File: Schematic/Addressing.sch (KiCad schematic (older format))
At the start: 6 parts, among them IC10 74LS593, IC11 74LS153, IC7 74LS574, IC8 74LS574, IC9 74LS593, U1 QX14T50B1.843200B50TT

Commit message: Fixed up some schematic DCN mistakes and also a few minor typos and diagram issues.
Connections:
- net labels added: adr[0..15], d[0..7]
- net labels removed: AddressBus, DataBus
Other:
- note added: "AddressBus"
- note added: "DataBus"
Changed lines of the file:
@@
 	5600 5100 5550 5100
 $Comp
-L GNDREF #PWR025
+L GNDREF #PWR020
 U 1 1 5C911F8E
 P 7000 6150
-F 0 "#PWR025" H 7000 5900 50  0001 C CNN
+F 0 "#PWR020" H 7000 5900 50  0001 C CNN
 F 1 "GNDREF" H 7000 6000 50  0000 C CNN
 F 2 "" H 7000 6150 50  0001 C CNN
@@
 $EndComp
 $Comp
-L VCC #PWR026
+L VCC #PWR021
 U 1 1 5C911FB4
 P 7000 6000
-F 0 "#PWR026" H 7000 5850 50  0001 C CNN
+F 0 "#PWR021" H 7000 5850 50  0001 C CNN
 F 1 "VCC" H 7000 6150 50  0000 C CNN
 F 2 "" H 7000 6000 50  0001 C CNN
@@
 $EndComp
 $Comp
-L VCC #PWR027
+L VCC #PWR022
 U 1 1 5C913009
 P 5550 4600
-F 0 "#PWR027" H 5550 4450 50  0001 C CNN
+F 0 "#PWR022" H 5550 4450 50  0001 C CNN
 F 1 "VCC" H 5550 4750 50  0000 C CNN
 F 2 "" H 5550 4600 50  0001 C CNN
@@
 	3000 6150 4450 6150
 $Comp
-L GNDREF #PWR028
+L GNDREF #PWR023
 U 1 1 5C90C705
 P 1800 6250
-F 0 "#PWR028" H 1800 6000 50  0001 C CNN
+F 0 "#PWR023" H 1800 6000 50  0001 C CNN
 F 1 "GNDREF" H 1800 6100 50  0000 C CNN
 F 2 "" H 1800 6250 50  0001 C CNN
@@
 	3000 6450 3200 6450
 $Comp
-L VCC #PWR029
+L VCC #PWR024
 U 1 1 5C90C821
 P 3200 6450
-F 0 "#PWR029" H 3200 6300 50  0001 C CNN
+F 0 "#PWR024" H 3200 6300 50  0001 C CNN
 F 1 "VCC" H 3200 6600 50  0000 C CNN
 F 2 "" H 3200 6450 50  0001 C CNN
@@
 	1    0    0    -1
 $EndComp
-Text GLabel 1250 650  0    60   Input ~ 0
-AddressBus
 $Comp
 L 74LS574-RESCUE-Schematic IC7
@@
 Wire Bus Line
 	1950 4900 1200 4900
-Text GLabel 1200 4900 0    60   Input ~ 0
-DataBus
 Entry Wire Line
 	1950 3300 2050 3200
@@
 d7
 $Comp
-L VCC #PWR035
+L VCC #PWR025
 U 1 1 5C99A807
 P 3850 2150
-F 0 "#PWR035" H 3850 2000 50  0001 C CNN
+F 0 "#PWR025" H 3850 2000 50  0001 C CNN
 F 1 "VCC" H 3850 2300 50  0000 C CNN
 F 2 "" H 3850 2150 50  0001 C CNN
@@
 $EndComp
 $Comp
-L VCC #PWR036
+L VCC #PWR026
 U 1 1 5C99A830
 P 3850 4100
-F 0 "#PWR036" H 3850 3950 50  0001 C CNN
+F 0 "#PWR026" H 3850 3950 50  0001 C CNN
 F 1 "VCC" H 3850 4250 50  0000 C CNN
 F 2 "" H 3850 4100 50  0001 C CNN
@@
 $EndComp
 $Comp
-L GNDREF #PWR038
+L GNDREF #PWR027
 U 1 1 5C99A88B
 P 3850 2250
-F 0 "#PWR038" H 3850 2000 50  0001 C CNN
+F 0 "#PWR027" H 3850 2000 50  0001 C CNN
 F 1 "GNDREF" H 3850 2100 50  0000 C CNN
 F 2 "" H 3850 2250 50  0001 C CNN
@@
 $EndComp
 $Comp
-L GNDREF #PWR039
+L GNDREF #PWR028
 U 1 1 5C99AB18
 P 3850 4200
-F 0 "#PWR039" H 3850 3950 50  0001 C CNN
+F 0 "#PWR028" H 3850 3950 50  0001 C CNN
 F 1 "GNDREF" H 3850 4050 50  0000 C CNN
 F 2 "" H 3850 4200 50  0001 C CNN
@@
 	4100 3800 5650 3800
 Wire Bus Line
-	4000 650  1250 650
+	4000 650  3350 650
 Wire Wire Line
 	4100 1250 5650 1250
@@
 Connection ~ 4400 2150
 $Comp
-L VCC #PWR?
+L VCC #PWR029
 U 1 1 5C9A1A2E
 P 7300 1250
-F 0 "#PWR?" H 7300 1100 50  0001 C CNN
+F 0 "#PWR029" H 7300 1100 50  0001 C CNN
 F 1 "VCC" H 7300 1400 50  0000 C CNN
 F 2 "" H 7300 1250 50  0001 C CNN
@@
 NoConn ~ 7000 1250
 $Comp
-L GNDREF #PWR?
+L GNDREF #PWR030
 U 1 1 5C9A1C76
 P 7300 4200
-F 0 "#PWR?" H 7300 3950 50  0001 C CNN
+F 0 "#PWR030" H 7300 3950 50  0001 C CNN
 F 1 "GNDREF" H 7300 4050 50  0000 C CNN
 F 2 "" H 7300 4200 50  0001 C CNN
@@
 Connection ~ 7300 3600
 $Comp
-L GNDREF #PWR?
+L GNDREF #PWR031
 U 1 1 5C9A1E6F
 P 7300 2050
-F 0 "#PWR?" H 7300 1800 50  0001 C CNN
+F 0 "#PWR031" H 7300 1800 50  0001 C CNN
 F 1 "GNDREF" H 7300 1900 50  0000 C CNN
 F 2 "" H 7300 2050 50  0001 C CNN
@@
 	7450 1950 7450 3900
 $Comp
-L VCC #PWR?
+L VCC #PWR032
 U 1 1 5C9A2F13
 P 7300 3200
-F 0 "#PWR?" H 7300 3050 50  0001 C CNN
+F 0 "#PWR032" H 7300 3050 50  0001 C CNN
 F 1 "VCC" H 7300 3350 50  0000 C CNN
 F 2 "" H 7300 3200 50  0001 C CNN
@@
 Text Notes 6250 3550 0    60   ~ 0
 PClo
+Text GLabel 1200 4900 0    60   Input ~ 0
+d[0..7]
+Text GLabel 3350 650  0    60   Input ~ 0
+adr[0..15]
+Text Notes 1400 4850 0    60   ~ 0
+DataBus
+Text Notes 3450 600  0    60   ~ 0
+AddressBus
 $EndSCHEMATC

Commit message: Working on the PCB
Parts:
- IC10, IC7, IC8, IC9: footprint (none) -> Housings_DIP:DIP-20_W7.62mm_Socket
- IC11: footprint (none) -> Housings_DIP:DIP-16_W7.62mm_Socket
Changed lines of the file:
@@
 F 0 "IC11" H 6350 6400 50  0000 C CNN
 F 1 "74LS153" H 6350 6300 50  0000 C CNN
-F 2 "" H 6350 5500 50  0001 C CNN
+F 2 "Housings_DIP:DIP-16_W7.62mm_Socket" H 6350 5500 50  0001 C CNN
 F 3 "" H 6350 5500 50  0001 C CNN
 	1    6350 5500
@@
 F 0 "IC7" H 3000 2450 50  0000 C CNN
 F 1 "74LS574" H 3000 2350 50  0000 C CNN
-F 2 "" H 3000 1750 50  0001 C CNN
+F 2 "Housings_DIP:DIP-20_W7.62mm_Socket" H 3000 1750 50  0001 C CNN
 F 3 "" H 3000 1750 50  0001 C CNN
 	1    3000 1750
@@
 F 0 "IC8" H 2950 4400 50  0000 C CNN
 F 1 "74LS574" H 2950 4300 50  0000 C CNN
-F 2 "" H 2950 3700 50  0001 C CNN
+F 2 "Housings_DIP:DIP-20_W7.62mm_Socket" H 2950 3700 50  0001 C CNN
 F 3 "" H 2950 3700 50  0001 C CNN
 	1    2950 3700
@@
 F 0 "IC9" H 6350 2400 50  0000 C CNN
 F 1 "74LS593" H 6350 2300 50  0000 C CNN
-F 2 "" H 6350 1700 50  0001 C CNN
+F 2 "Housings_DIP:DIP-20_W7.62mm_Socket" H 6350 1700 50  0001 C CNN
 F 3 "" H 6350 1700 50  0001 C CNN
 	1    6350 1700
@@
 F 0 "IC10" H 6350 4350 50  0000 C CNN
 F 1 "74LS593" H 6350 4250 50  0000 C CNN
-F 2 "" H 6350 3650 50  0001 C CNN
+F 2 "Housings_DIP:DIP-20_W7.62mm_Socket" H 6350 3650 50  0001 C CNN
 F 3 "" H 6350 3650 50  0001 C CNN
 	1    6350 3650

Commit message: Added a reset circuit and a single-step clock circuit to the schematic, as well as the bypass capacitors. Also, got used to the PCB creation workflow.
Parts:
- removed U1: QX14T50B1.843200B50TT, Oscillators:Oscillator_DIP-14, symbol QX14T50B1.843200B50TT
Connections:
- net labels added: Reset
- wire segments 106 -> 105
- no-connect marks 7 -> 6
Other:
- note removed: "Clk"
- note removed: "Clock\n Xtal"
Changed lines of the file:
@@
 $Descr A4 11693 8268
 encoding utf-8
-Sheet 4 5
+Sheet 4 6
 Title ""
 Date ""
@@
 Wire Wire Line
 	5550 4800 5550 4600
-$Comp
-L QX14T50B1.843200B50TT U1
-U 1 1 5C90C424
-P 1800 6150
-F 0 "U1" H 2350 6400 50  0000 L CNN
-F 1 "QX14T50B1.843200B50TT" H 1950 6300 50  0000 L CNN
-F 2 "Oscillators:Oscillator_DIP-14" H 2850 6250 50  0001 L CNN
-F 3 "http://docs-emea.rs-online.com/webdocs/127f/0900766b8127fc57.pdf" H 2850 6150 50  0001 L CNN
-F 4 "QX14T50B1.843200B50TT, Crystal Oscillator, 1.8432 MHz, +/-50ppm HCMOS 50pF, 14-pin PDIP, 20.8 x 13.2 x 5.08mm" H 2850 6050 50  0001 L CNN "Description"
-F 5 "" H 2850 5950 50  0001 L CNN "Height"
-F 6 "Qantek" H 2850 5850 50  0001 L CNN "Manufacturer_Name"
-F 7 "QX14T50B1.843200B50TT" H 2850 5750 50  0001 L CNN "Manufacturer_Part_Number"
-F 8 "" H 2850 5650 50  0001 L CNN "Mouser Part Number"
-F 9 "" H 2850 5550 50  0001 L CNN "Mouser Price/Stock"
-F 10 "1735868" H 2850 5450 50  0001 L CNN "RS Part Number"
-F 11 "http://uk.rs-online.com/web/p/products/1735868" H 2850 5350 50  0001 L CNN "RS Price/Stock"
-F 12 "70418025" H 2850 5250 50  0001 L CNN "Allied_Number"
-F 13 "http://www.alliedelec.com/qantek-qx14t50b18-43200b50tt/70418025/" H 2850 5150 50  0001 L CNN "Allied Price/Stock"
-	1    1800 6150
-	1    0    0    -1
-$EndComp
-Wire Wire Line
-	3000 6150 4450 6150
-$Comp
-L GNDREF #PWR023
-U 1 1 5C90C705
-P 1800 6250
-F 0 "#PWR023" H 1800 6000 50  0001 C CNN
-F 1 "GNDREF" H 1800 6100 50  0000 C CNN
-F 2 "" H 1800 6250 50  0001 C CNN
-F 3 "" H 1800 6250 50  0001 C CNN
-	1    1800 6250
-	1    0    0    -1
-$EndComp
-Wire Wire Line
-	3000 6250 3000 6450
-Wire Wire Line
-	3000 6450 3200 6450
-$Comp
-L VCC #PWR024
-U 1 1 5C90C821
-P 3200 6450
-F 0 "#PWR024" H 3200 6300 50  0001 C CNN
-F 1 "VCC" H 3200 6600 50  0000 C CNN
-F 2 "" H 3200 6450 50  0001 C CNN
-F 3 "" H 3200 6450 50  0001 C CNN
-	1    3200 6450
-	1    0    0    -1
-$EndComp
-Text Notes 3250 6100 0    60   ~ 0
-Clk
-NoConn ~ 1800 6150
-Text Notes 2250 6550 0    60   ~ 0
-Clock\n Xtal
 $Comp
 L 74LS153-RESCUE-Schematic U?
@@
 d7
 $Comp
-L VCC #PWR025
+L VCC #PWR023
 U 1 1 5C99A807
 P 3850 2150
-F 0 "#PWR025" H 3850 2000 50  0001 C CNN
+F 0 "#PWR023" H 3850 2000 50  0001 C CNN
 F 1 "VCC" H 3850 2300 50  0000 C CNN
 F 2 "" H 3850 2150 50  0001 C CNN
@@
 $EndComp
 $Comp
-L VCC #PWR026
+L VCC #PWR024
 U 1 1 5C99A830
 P 3850 4100
-F 0 "#PWR026" H 3850 3950 50  0001 C CNN
+F 0 "#PWR024" H 3850 3950 50  0001 C CNN
 F 1 "VCC" H 3850 4250 50  0000 C CNN
 F 2 "" H 3850 4100 50  0001 C CNN
@@
 $EndComp
 $Comp
-L GNDREF #PWR027
+L GNDREF #PWR025
 U 1 1 5C99A88B
 P 3850 2250
-F 0 "#PWR027" H 3850 2000 50  0001 C CNN
+F 0 "#PWR025" H 3850 2000 50  0001 C CNN
 F 1 "GNDREF" H 3850 2100 50  0000 C CNN
 F 2 "" H 3850 2250 50  0001 C CNN
@@
 $EndComp
 $Comp
-L GNDREF #PWR028
+L GNDREF #PWR026
 U 1 1 5C99AB18
 P 3850 4200
-F 0 "#PWR028" H 3850 3950 50  0001 C CNN
+F 0 "#PWR026" H 3850 3950 50  0001 C CNN
 F 1 "GNDREF" H 3850 4050 50  0000 C CNN
 F 2 "" H 3850 4200 50  0001 C CNN
@@
 Wire Wire Line
 	3850 2250 3600 2250
-Text GLabel 4450 6150 2    60   Input ~ 0
+Text GLabel 4100 4850 0    60   Input ~ 0
 Clk
 Wire Wire Line
@@
 	4400 4000 5650 4000
 Wire Wire Line
-	4400 2050 4400 6150
-Connection ~ 4400 6150
-Wire Wire Line
 	5650 4100 4400 4100
 Connection ~ 4400 4100
@@
 Connection ~ 4400 2150
 $Comp
-L VCC #PWR029
+L VCC #PWR027
 U 1 1 5C9A1A2E
 P 7300 1250
-F 0 "#PWR029" H 7300 1100 50  0001 C CNN
+F 0 "#PWR027" H 7300 1100 50  0001 C CNN
 F 1 "VCC" H 7300 1400 50  0000 C CNN
 F 2 "" H 7300 1250 50  0001 C CNN
@@
 	7300 1250 7300 1550
 Wire Wire Line
-	7000 1350 7300 1350
-Connection ~ 7300 1350
-Wire Wire Line
 	7300 1550 6950 1550
 Connection ~ 7300 1450
 NoConn ~ 7000 1250
 $Comp
-L GNDREF #PWR030
+L GNDREF #PWR028
 U 1 1 5C9A1C76
 P 7300 4200
-F 0 "#PWR030" H 7300 3950 50  0001 C CNN
+F 0 "#PWR028" H 7300 3950 50  0001 C CNN
 F 1 "GNDREF" H 7300 4050 50  0000 C CNN
 F 2 "" H 7300 4200 50  0001 C CNN
@@
 Connection ~ 7300 3600
 $Comp
-L GNDREF #PWR031
+L GNDREF #PWR029
 U 1 1 5C9A1E6F
 P 7300 2050
-F 0 "#PWR031" H 7300 1800 50  0001 C CNN
+F 0 "#PWR029" H 7300 1800 50  0001 C CNN
 F 1 "GNDREF" H 7300 1900 50  0000 C CNN
 F 2 "" H 7300 2050 50  0001 C CNN
@@
 	7450 1950 7450 3900
 $Comp
-L VCC #PWR032
+L VCC #PWR030
 U 1 1 5C9A2F13
 P 7300 3200
-F 0 "#PWR032" H 7300 3050 50  0001 C CNN
+F 0 "#PWR030" H 7300 3050 50  0001 C CNN
 F 1 "VCC" H 7300 3350 50  0000 C CNN
 F 2 "" H 7300 3200 50  0001 C CNN
@@
 Wire Wire Line
 	7300 3200 7300 3500
-Wire Wire Line
-	7000 3300 7300 3300
-Connection ~ 7300 3300
 Wire Wire Line
 	7300 3500 6950 3500
@@
 Text Notes 3450 600  0    60   ~ 0
 AddressBus
+Wire Wire Line
+	4400 2050 4400 4850
+Wire Wire Line
+	4400 4850 4100 4850
+Text GLabel 7800 1350 2    60   Input ~ 0
+Reset
+Wire Wire Line
+	7000 1350 7800 1350
+Wire Wire Line
+	7000 3300 7600 3300
+Wire Wire Line
+	7600 3300 7600 1350
+Connection ~ 7600 1350
 $EndSCHEMATC

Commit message: Brought the schematic and PCB board design up to date.
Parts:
- removed IC11: 74LS153, Housings_DIP:DIP-16_W7.62mm_Socket, symbol 74LS153-RESCUE-Schematic
- added IC11: 74HCT251, Housings_DIP:DIP-16_W7.62mm_Socket, symbol 74LS251-RESCUE-Schematic
- IC7, IC8: value 74LS574 -> 74HCT574
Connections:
- net labels added: DivByZero, Hi, JumpOp0, JumpOp1, JumpOp2, JumpOp[0..2], Lo, Overflow, PCload, ~ARena, ~PCload, ~RXready, ~Reset, ~TXready
- net labels removed: ARena, Clk, JumpC, JumpZ, Reset
- wire segments 105 -> 111
- no-connect marks 6 -> 1
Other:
- note added: "The address bus value, which goes to the RAM & ROM,\ncomes either from the Address register (ARhi, ARlo)\nor the Program Counter (PChi, PClo). The ARena line\nenables one and disables the other.\n\nThe address register loads from the databus, using\nthe AHload and ALload control lines.\n\nThe PC can keep its current value, increment on\nPCincr or load when the /Z line (pin 6) from the\nJump logic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"
- note removed: "NoJump"

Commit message: Brought the schematic up to date with the wiring from the TTL verilog version.
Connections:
- net Hi: now also IC10.14 (CCKEN#); no longer IC9.15 (CCKEN)
- net Lo: no longer IC10.14 (CCKEN#)
- net PCincr: now also IC9.15 (CCKEN); no longer IC10.13 (CCK), IC9.13 (CCK)
- new net ~Clkbar: IC10.13 (CCK), IC9.13 (CCK)
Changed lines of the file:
@@
 Text GLabel 7950 3900 2    60   Input ~ 0
 ~ARena
-Text GLabel 4950 4100 0    60   Input ~ 0
-PCincr
 $Comp
 L VCC #PWR023
@@
 Wire Wire Line
 	5100 5450 5450 5450
-Text GLabel 7100 1850 2    60   Input ~ 0
-Hi
 Wire Wire Line
 	8550 1550 8550 1300
@@
 Lo
 Text GLabel 7100 4100 2    60   Input ~ 0
-Lo
+Hi
 Text GLabel 5250 6050 0    60   Input ~ 0
 Lo
@@
 Wire Wire Line
 	7000 4100 7100 4100
+Wire Wire Line
+	7050 1850 7100 1850
+Text GLabel 4950 4100 0    60   Input ~ 0
+~Clkbar
 Text GLabel 7300 3800 2    60   Input ~ 0
 PCincr
-Wire Wire Line
-	7050 1850 7100 1850
 Text GLabel 4800 2150 0    60   Input ~ 0
+~Clkbar
+Text GLabel 7100 1850 2    60   Input ~ 0
 PCincr
 $EndSCHEMATC

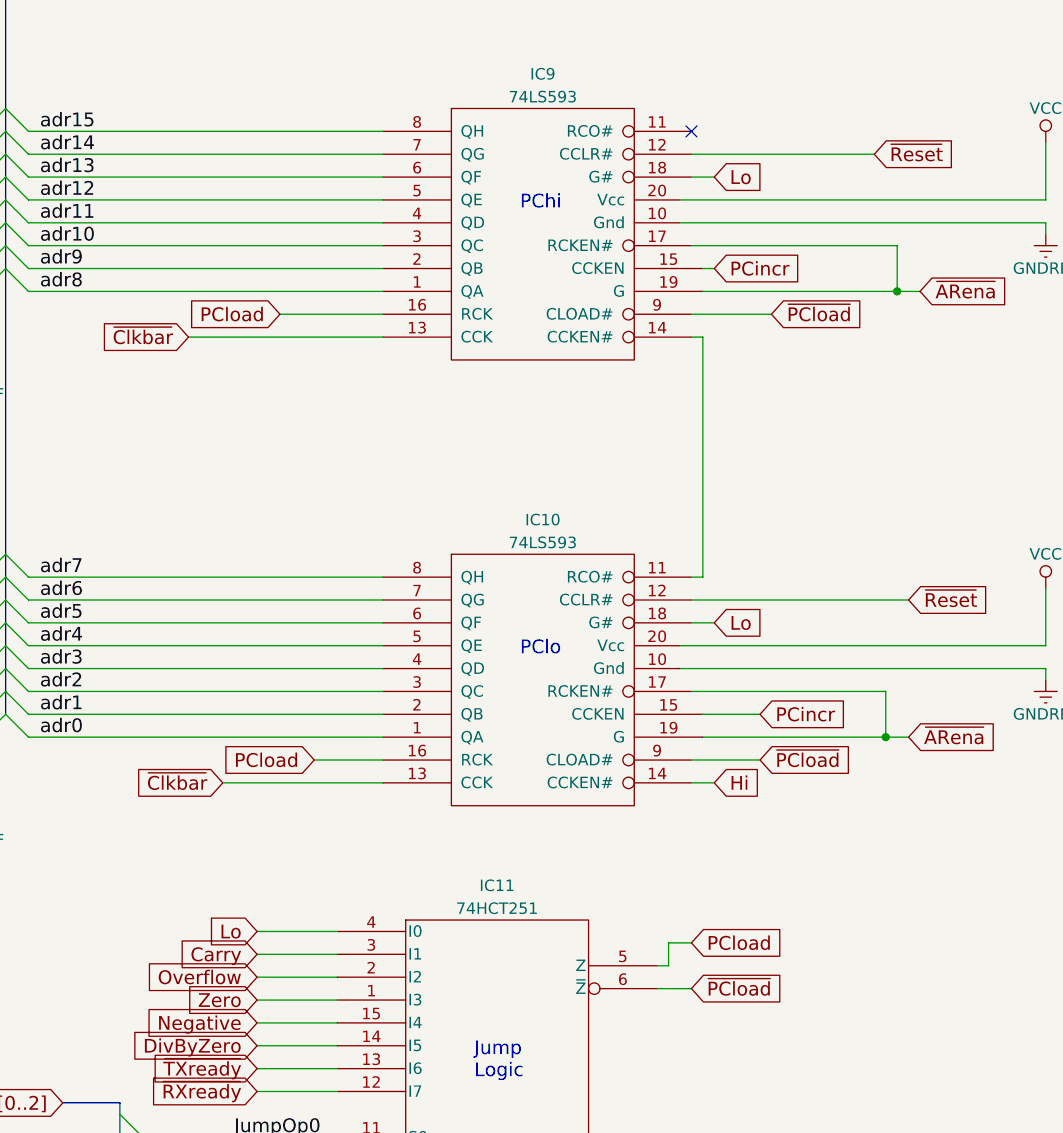
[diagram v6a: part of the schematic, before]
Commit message: Reworked the 74LS593 wiring in the KiCad schematic and updated my journal.
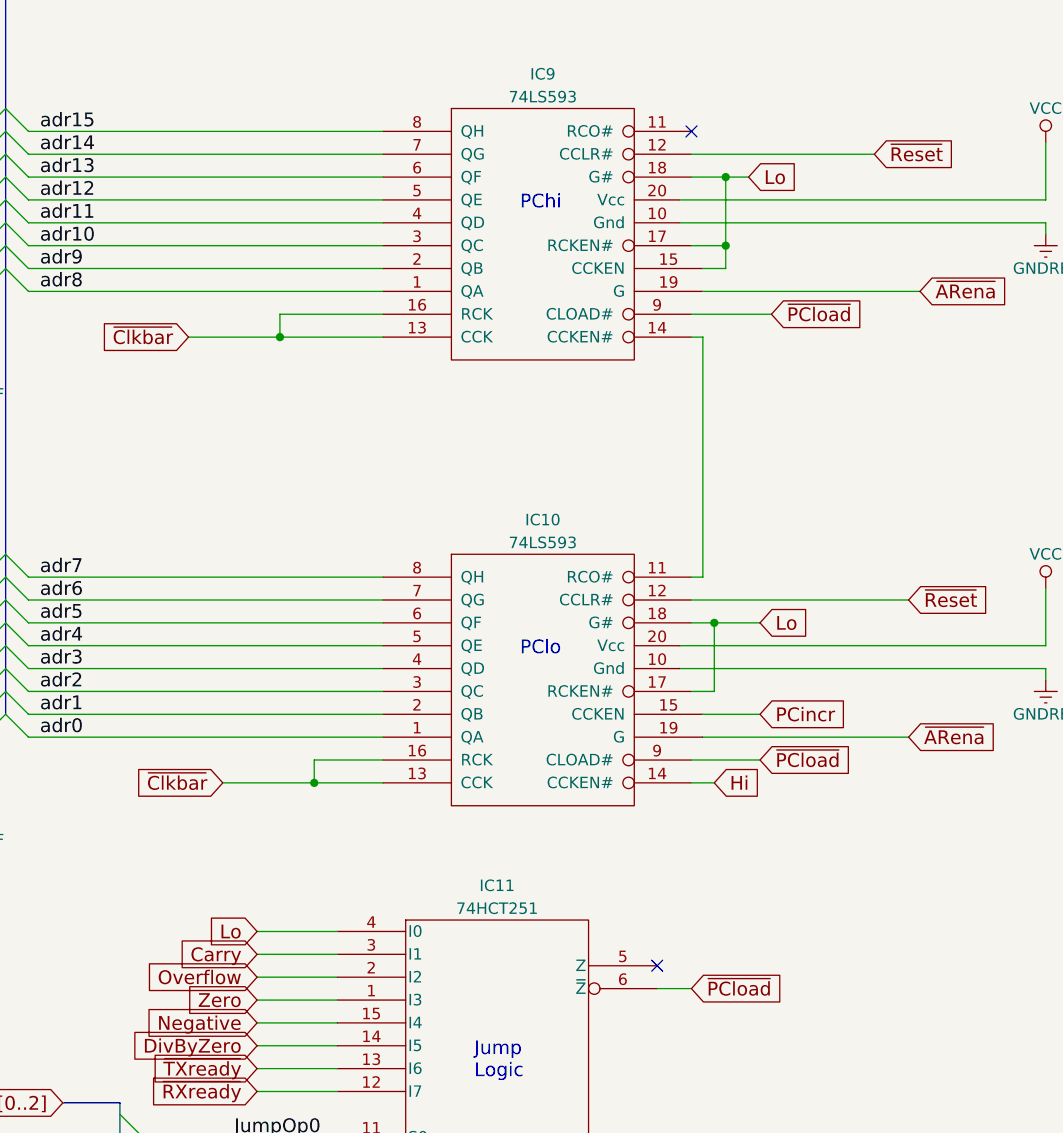
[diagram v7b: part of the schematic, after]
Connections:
- net Lo: now also IC10.17 (RCKEN#), IC9.15 (CCKEN), IC9.17 (RCKEN#)
- net PCincr: no longer IC9.15 (CCKEN)
- net ~ARena: no longer IC10.17 (RCKEN#), IC9.17 (RCKEN#)
- net ~Clkbar: now also IC10.16 (RCK), IC9.16 (RCK)
- removed net PCload: IC10.16 (RCK), IC11.5 (Z), IC9.16 (RCK)
- no-connect marks 1 -> 2
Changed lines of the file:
@@
 Wire Wire Line
 	6950 1650 8550 1650
-Text GLabel 7100 1450 2    60   Input ~ 0
+Text GLabel 7250 1450 2    60   Input ~ 0
 Lo
 Wire Wire Line
@@
 Wire Wire Line
 	8550 3600 8550 3650
-Text GLabel 7100 3400 2    60   Input ~ 0
+Text GLabel 7300 3400 2    60   Input ~ 0
 Lo
-Text GLabel 7100 4100 2    60   Input ~ 0
-Hi
 Text GLabel 5250 6050 0    60   Input ~ 0
 Lo
@@
 	7050 3900 7950 3900
 Wire Wire Line
-	7000 3700 7850 3700
-Wire Wire Line
-	7850 3700 7850 3900
-Connection ~ 7850 3900
-Wire Wire Line
 	7050 1950 8000 1950
-Wire Wire Line
-	7000 1750 7900 1750
-Wire Wire Line
-	7900 1750 7900 1950
-Connection ~ 7900 1950
-Text GLabel 7000 4800 2    60   Input ~ 0
-PCload
 Text GLabel 7000 5000 2    60   Input ~ 0
 ~PCload
 Wire Wire Line
 	6850 5000 7000 5000
-Wire Wire Line
-	7000 4800 6900 4800
-Wire Wire Line
-	6900 4800 6900 4900
-Wire Wire Line
-	6900 4900 6850 4900
 Text GLabel 7300 4000 2    60   Input ~ 0
 ~PCload
@@
 ~PCload
 Wire Wire Line
-	5200 2050 5650 2050
-Wire Wire Line
 	7000 2050 7350 2050
 Wire Wire Line
 	7000 4000 7300 4000
-Text GLabel 5350 4000 0    60   Input ~ 0
-PCload
-Text GLabel 5200 2050 0    60   Input ~ 0
-PCload
 Wire Wire Line
-	7000 3400 7100 3400
+	7000 3400 7300 3400
 Wire Wire Line
-	7000 1450 7100 1450
+	7000 1450 7250 1450
 Wire Wire Line
 	7000 1350 7800 1350
@@
 	7000 4100 7100 4100
 Wire Wire Line
-	7050 1850 7100 1850
+	7050 1850 7150 1850
 Text GLabel 4950 4100 0    60   Input ~ 0
 ~Clkbar
@@
 Text GLabel 4800 2150 0    60   Input ~ 0
 ~Clkbar
-Text GLabel 7100 1850 2    60   Input ~ 0
-PCincr
+NoConn ~ 6850 4900
+Wire Wire Line
+	5200 2050 5650 2050
+Text GLabel 7100 4100 2    60   Input ~ 0
+Hi
+Wire Wire Line
+	5200 2050 5200 2150
+Connection ~ 5200 2150
+Wire Wire Line
+	5350 4000 5350 4100
+Connection ~ 5350 4100
+Wire Wire Line
+	7000 3700 7100 3700
+Wire Wire Line
+	7100 3700 7100 3400
+Connection ~ 7100 3400
+Wire Wire Line
+	7150 1850 7150 1450
+Connection ~ 7150 1450
+Wire Wire Line
+	7000 1750 7150 1750
+Connection ~ 7150 1750
 $EndSCHEMATC
